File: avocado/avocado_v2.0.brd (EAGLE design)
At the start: 104.9 x 79 mm, 94 parts, among them IC1 TM4C129XXXPDT, IC3 MAX31855, IC4 ISO3088, J1 THERMOCOUPLE, U1 LMT87DCKT, U2 AS5048A-HTSP-500

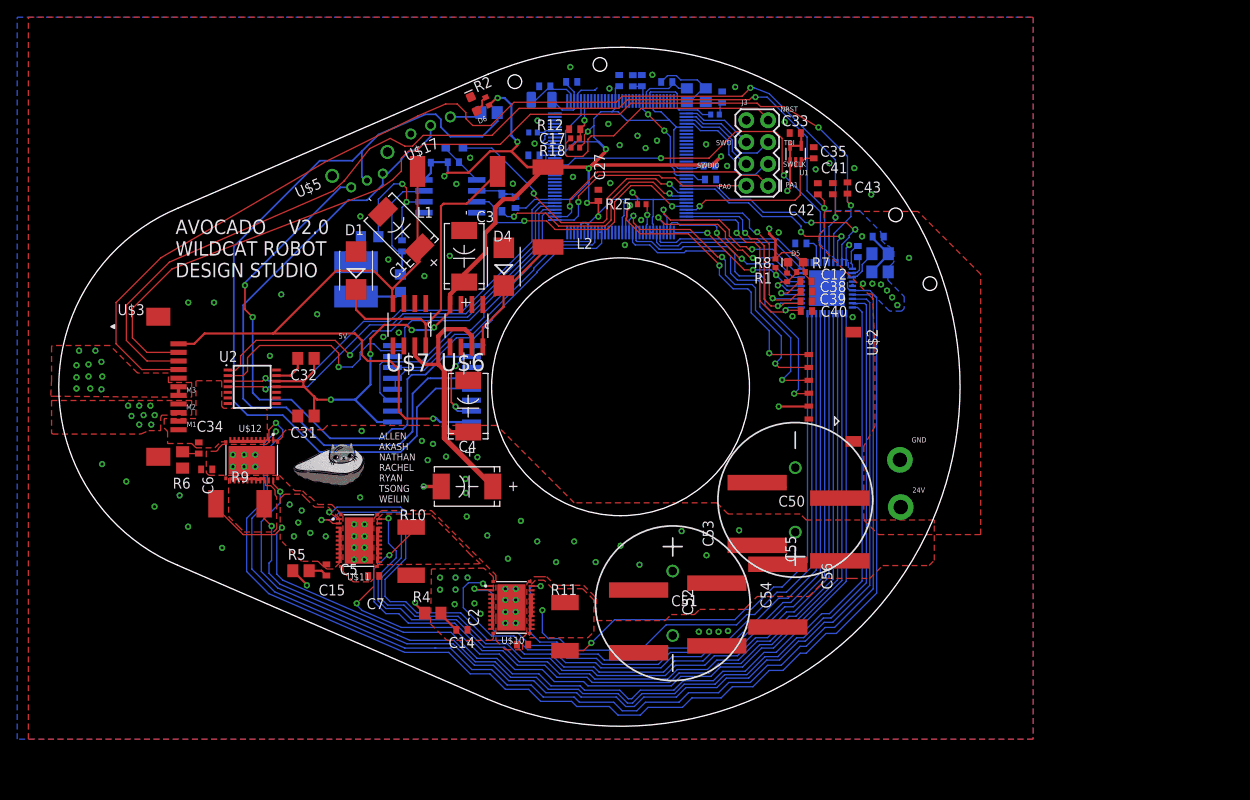
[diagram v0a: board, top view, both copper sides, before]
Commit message: added mounting holes to main pcb
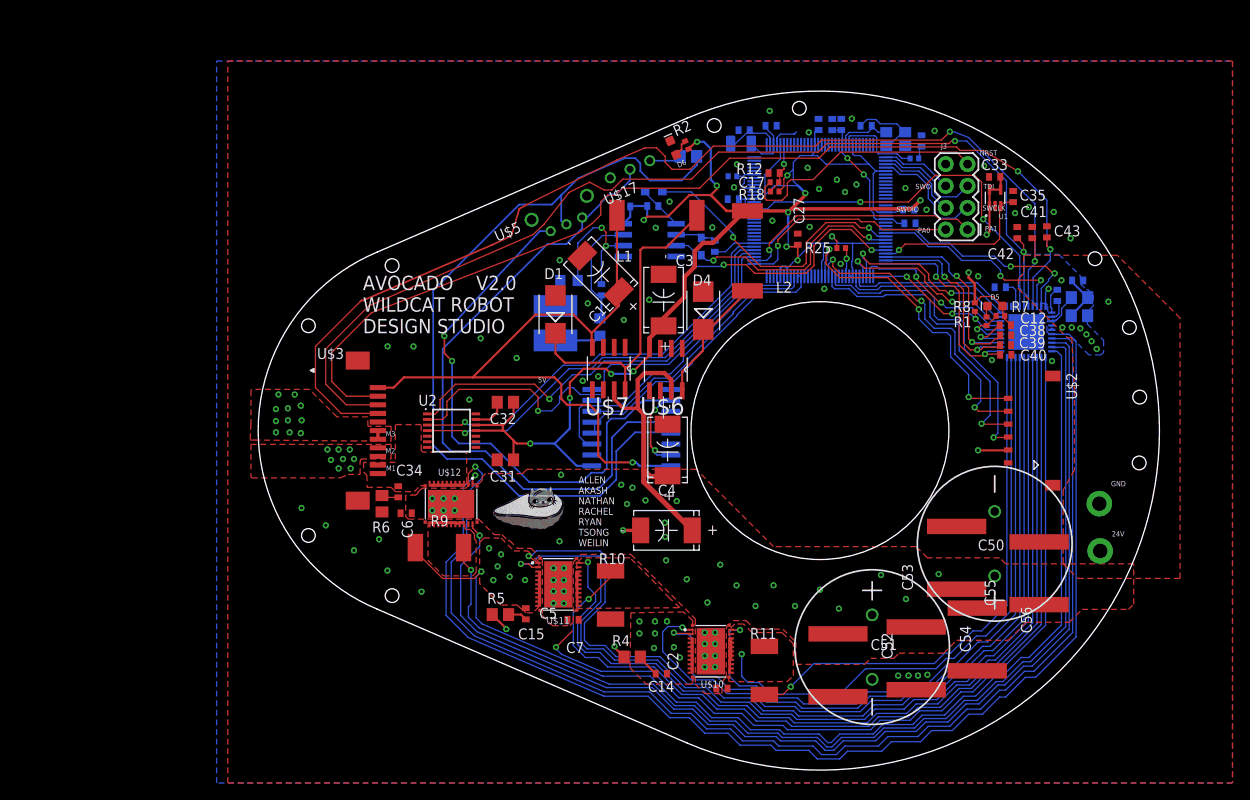
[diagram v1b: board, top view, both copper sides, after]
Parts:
- moved C11 23.8 mm to (104.5, 62.8)
- moved C22 23.8 mm to (82.3, 82.6)
- moved C24 23.8 mm to (68.1, 82.1)
- moved C25 23.8 mm to (71.2, 82.6)
- moved C28 23.8 mm to (87.2, 72.8)
- moved C35 23.8 mm to (99.4, 74.3)
- moved C7 23.8 mm to (65.5, 17.1)
- moved D1 23.8 mm to (46.1, 60.6)
- moved J3 23.8 mm to (92.8, 74.3)
- moved R14 23.8 mm to (87.9, 78.8)
- moved R34 23.8 mm to (64.7, 68.6)
- moved FB2 23.8 mm to (51.3, 59.1)
- moved U$5 23.8 mm to (47.4, 71.1)
- moved C1 23.8 mm to (51.4, 65.3)
- moved C12 23.8 mm to (98.5, 59.4)
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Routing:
- net H2: track 125.4 -> 126.4 mm

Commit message: version 2 of the avocado pcb finished
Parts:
- removed U$6: LM2594M-5.0, avocado:SOIC127P620X175-8N
- added C16: 0.01uF, rcl:C0402
- added U$8: LM2675M, avocado:SO08
- L2: value SRU1028 -> B82464G4473M000; device avocado:SRU1028 -> avocado:B82464G4473M000
- moved C3 20.1 mm to (68.4, 79.9)
- moved D4 4.08 mm to (59.3, 61.9)
- moved R16 3.80 mm to (58.5, 76.8), turned to 180 degrees
- moved L2 2.15 mm to (67.3, 66.2), turned to 45 degrees
- moved U$5 1.61 mm to (46.6, 72.5)
- moved U$17 0.92 mm to (54.2, 78.2)
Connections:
- new net N$4: C16.1, U$8.1
- net 24VDC: now also U$8.7; no longer U$6.7
- net 3V3DC: now also U$8.4; no longer U$6.4
- net GND: now also J3.8, U$8.6; no longer U$6.5, U$6.6
- net N$25: now also C16.2, U$8.8; no longer U$6.8
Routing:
- net B: track 97.2 -> 82.3 mm, vias 0 -> 2
- net 3V3DC: track 294.6 -> 306.7 mm, vias 17 -> 16
- net N$25: track 17.2 -> 22.5 mm
- net GND: track 303.8 -> 308.8 mm, vias 54 -> 56
- net VBAT: track 3.51 -> 0.00 mm
- net N$4: track 0.00 -> 3.07 mm
- net A: track 83.3 -> 86.2 mm
- net H2: track 126.4 -> 124.4 mm
- net PA0: track 26.3 -> 25.2 mm
- net N$24: track 38.9 -> 37.9 mm
- net 24VDC: track 42.3 -> 41.5 mm
- net N$23: track 3.76 -> 4.45 mm
- net GND_EXT: track 82.9 -> 83.2 mm, vias 4 -> 2

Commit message: latest gerbers and main pcb design
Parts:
- removed U2: AS5048A-HTSP-500, avocado:SOP65P640X120-14N
- added U$1: 5040500691, avocado:5040500691
- U$2: value 5040500691 -> AS5048A-HTSP-500; device avocado:5040500691 -> avocado:SOP65P640X120-14N
- moved U$2 64.8 mm to (34.0, 47.1), turned to 0 degrees
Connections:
- net 3V3DC: now also U$1.2, U$2.11, U$2.12; no longer U$2.2, U2.11, U2.12
- net GND: now also U$1.1, U$2.13; no longer U$2.1, U2.13
- net PA2: now also U$2.2; no longer U2.2
- net PA3: now also U$2.1; no longer U2.1
- net PA4: now also U$2.4; no longer U2.4
- net PA5: now also U$2.3; no longer U2.3
- net PE0: now also U$1.6; no longer U$2.6
- net PE1: now also U$1.5; no longer U$2.5
- net PE2: now also U$1.4; no longer U$2.4
- net PE3: now also U$1.3; no longer U$2.3
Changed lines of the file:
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@@
 <attribute name="SPICEPREFIX" value="R" x="40.4" y="91.200003125" size="1.778" layer="28" rot="MR180" display="off"/>
 </element>
-<element name="U2" library="avocado" package="SOP65P640X120-14N" value="AS5048A-HTSP-500" x="34.0375" y="47.1">
+<element name="U$2" library="avocado" package="SOP65P640X120-14N" value="AS5048A-HTSP-500" x="34.0375" y="47.1">
 <attribute name="AVAILABILITY" value="Unavailable" x="24.9375" y="70.5" size="1.778" layer="27" display="off"/>
 <attribute name="DESCRIPTION" value=" AS5048B Series 360° 3.3 / 5 V 14 bit Magnetic Rotary Encoder - TSSOP-14 " x="24.9375" y="70.5" size="1.778" layer="27" display="off"/>
@@
 <attribute name="SPICEPREFIX" value="C" x="53.8" y="33.2" size="1.778" layer="27" rot="R180" display="off"/>
 </element>
-<element name="U$2" library="avocado" package="5040500691" value="5040500691" x="98.8" y="47.1" rot="R270"/>
+<element name="U$1" library="avocado" package="5040500691" value="5040500691" x="98.8" y="47.1" rot="R270"/>
 <element name="C16" library="rcl" library_urn="urn:adsk.eagle:library:334" package="C0402" package3d_urn="urn:adsk.eagle:package:23626/1" value="0.01uF" x="62.3" y="59.9" smashed="yes" rot="R90">
 <attribute name="NAME" x="63.335" y="61.035" size="1.27" layer="25" rot="R270"/>
@@
 <via x="88.3" y="18.6" extent="1-16" drill="0.35"/>
 <via x="89.4" y="18.7" extent="1-16" drill="0.35"/>
-<contactref element="U2" pad="13"/>
+<contactref element="U$2" pad="13"/>
 <contactref element="C31" pad="2"/>
 <contactref element="C32" pad="2"/>
-<contactref element="U$2" pad="1"/>
+<contactref element="U$1" pad="1"/>
 <wire x1="37.6" y1="24.6" x2="51.648509375" y2="18.529878125" width="0.1524" layer="16"/>
 <wire x1="37.6" y1="24.6" x2="36.9" y2="25.3" width="0.1524" layer="16"/>
@@
 <wire x1="47.8" y1="52.7" x2="49.4" y2="54.3" width="0.3048" layer="1"/>
 <wire x1="49.4" y1="54.3" x2="52" y2="54.3" width="0.3048" layer="1"/>
-<contactref element="U2" pad="12"/>
+<contactref element="U$2" pad="12"/>
 <contactref element="C31" pad="1"/>
-<contactref element="U2" pad="11"/>
+<contactref element="U$2" pad="11"/>
 <contactref element="C32" pad="1"/>
-<contactref element="U$2" pad="2"/>
+<contactref element="U$1" pad="2"/>
 <wire x1="59.2" y1="72" x2="61.7" y2="74.5" width="0.3048" layer="1"/>
 <wire x1="61.7" y1="74.5" x2="64.2" y2="74.5" width="0.3048" layer="1"/>
@@
 <wire x1="90.7" y1="60" x2="93.3" y2="60" width="0.1524" layer="16"/>
 <wire x1="93.7" y1="56.6" x2="97.6" y2="52.7" width="0.1524" layer="16"/>
-<contactref element="U$2" pad="3"/>
+<contactref element="U$1" pad="3"/>
 <wire x1="97.6" y1="46.8" x2="97.1" y2="46.3" width="0.1524" layer="16"/>
 <via x="97.1" y="46.3" extent="1-16" drill="0.35"/>
@@
 <wire x1="89.7" y1="60.3" x2="90.5" y2="59.5" width="0.1524" layer="16"/>
 <wire x1="90.5" y1="59.5" x2="92.9" y2="59.5" width="0.1524" layer="16"/>
-<contactref element="U$2" pad="4"/>
+<contactref element="U$1" pad="4"/>
 <wire x1="93.1" y1="56.4" x2="96.7" y2="52.8" width="0.1524" layer="16"/>
 <wire x1="96.7" y1="48.9" x2="95.7" y2="47.9" width="0.1524" layer="16"/>
@@
 <wire x1="78.4" y1="66.2" x2="79.2" y2="65.4" width="0.1524" layer="1"/>
 <wire x1="79.2" y1="65.4" x2="85" y2="65.4" width="0.1524" layer="1"/>
-<contactref element="U$2" pad="5"/>
+<contactref element="U$1" pad="5"/>
 <wire x1="95.6" y1="53" x2="95.6" y2="50.5" width="0.1524" layer="16"/>
 <wire x1="95.6" y1="50.5" x2="94.9" y2="49.8" width="0.1524" layer="16"/>
@@
 <wire x1="77.6" y1="67.5" x2="77.6" y2="66.5" width="0.1524" layer="1"/>
 <wire x1="77.6" y1="66.5" x2="79.2" y2="64.9" width="0.1524" layer="1"/>
-<contactref element="U$2" pad="6"/>
+<contactref element="U$1" pad="6"/>
 <wire x1="94.2" y1="53.6" x2="94.2" y2="51" width="0.1524" layer="16"/>
 <via x="94.2" y="51" extent="1-16" drill="0.35"/>
@@
 <wire x1="68.1" y1="67.3" x2="69.25" y2="67.3" width="0.1524" layer="16"/>
 <wire x1="67.8" y1="67" x2="68.1" y2="67.3" width="0.1524" layer="16"/>
-<contactref element="U2" pad="2"/>
+<contactref element="U$2" pad="2"/>
 <wire x1="47.6" y1="52.1" x2="46.6" y2="51.1" width="0.1524" layer="16"/>
 <wire x1="45.7" y1="49.4" x2="44.1" y2="49.4" width="0.1524" layer="16"/>
@@
 <wire x1="50.2" y1="53.6" x2="51.8" y2="55.2" width="0.1524" layer="16"/>
 <wire x1="51.8" y1="55.2" x2="59.1" y2="55.2" width="0.1524" layer="16"/>
-<contactref element="U2" pad="1"/>
+<contactref element="U$2" pad="1"/>
 <wire x1="31.2625" y1="49" x2="31.2125" y2="49.05" width="0.1524" layer="1"/>
 <wire x1="48.1" y1="53.6" x2="45.420925" y2="50.920925" width="0.1524" layer="16"/>
@@
 <wire x1="51.6" y1="55.6" x2="50.3" y2="54.3" width="0.1524" layer="16"/>
 <wire x1="47.7" y1="54.3" x2="47.6764" y2="54.3" width="0.1524" layer="16"/>
-<contactref element="U2" pad="4"/>
+<contactref element="U$2" pad="4"/>
 <wire x1="47.7" y1="54.3" x2="50.3" y2="54.3" width="0.1524" layer="16"/>
 <wire x1="47.7" y1="54.3" x2="40.5" y2="47.1" width="0.1524" layer="16"/>
@@
 <wire x1="51.3" y1="56" x2="50" y2="54.7" width="0.1524" layer="16"/>
 <wire x1="50" y1="54.7" x2="47" y2="54.7" width="0.1524" layer="16"/>
-<contactref element="U2" pad="3"/>
+<contactref element="U$2" pad="3"/>
 <wire x1="40.1" y1="47.8" x2="47" y2="54.7" width="0.1524" layer="16"/>
 <wire x1="35.6" y1="48.1" x2="35.9" y2="47.8" width="0.1524" layer="16"/>
